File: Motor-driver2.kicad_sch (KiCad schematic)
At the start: 30 parts, among them J12 PINHD_1x4_Male, J15 PINHD_1x4_Male, U4 DRV8825PWP, U5 DRV8825PWP

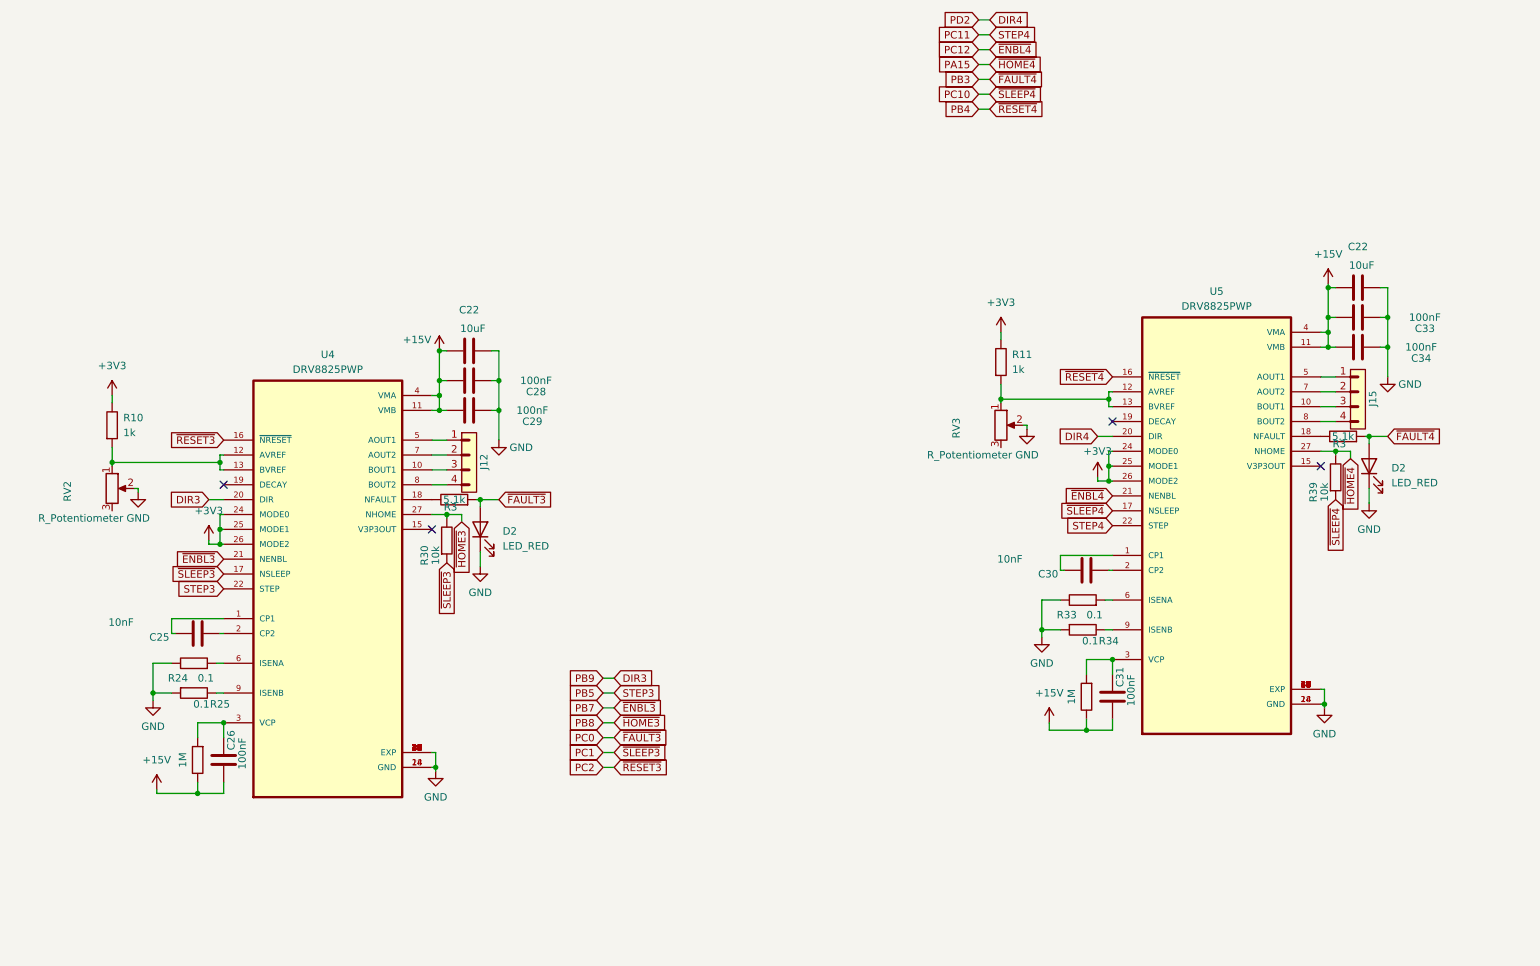
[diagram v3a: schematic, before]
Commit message: placed jlcpcb basic buttons and rerouted unchristliche wires
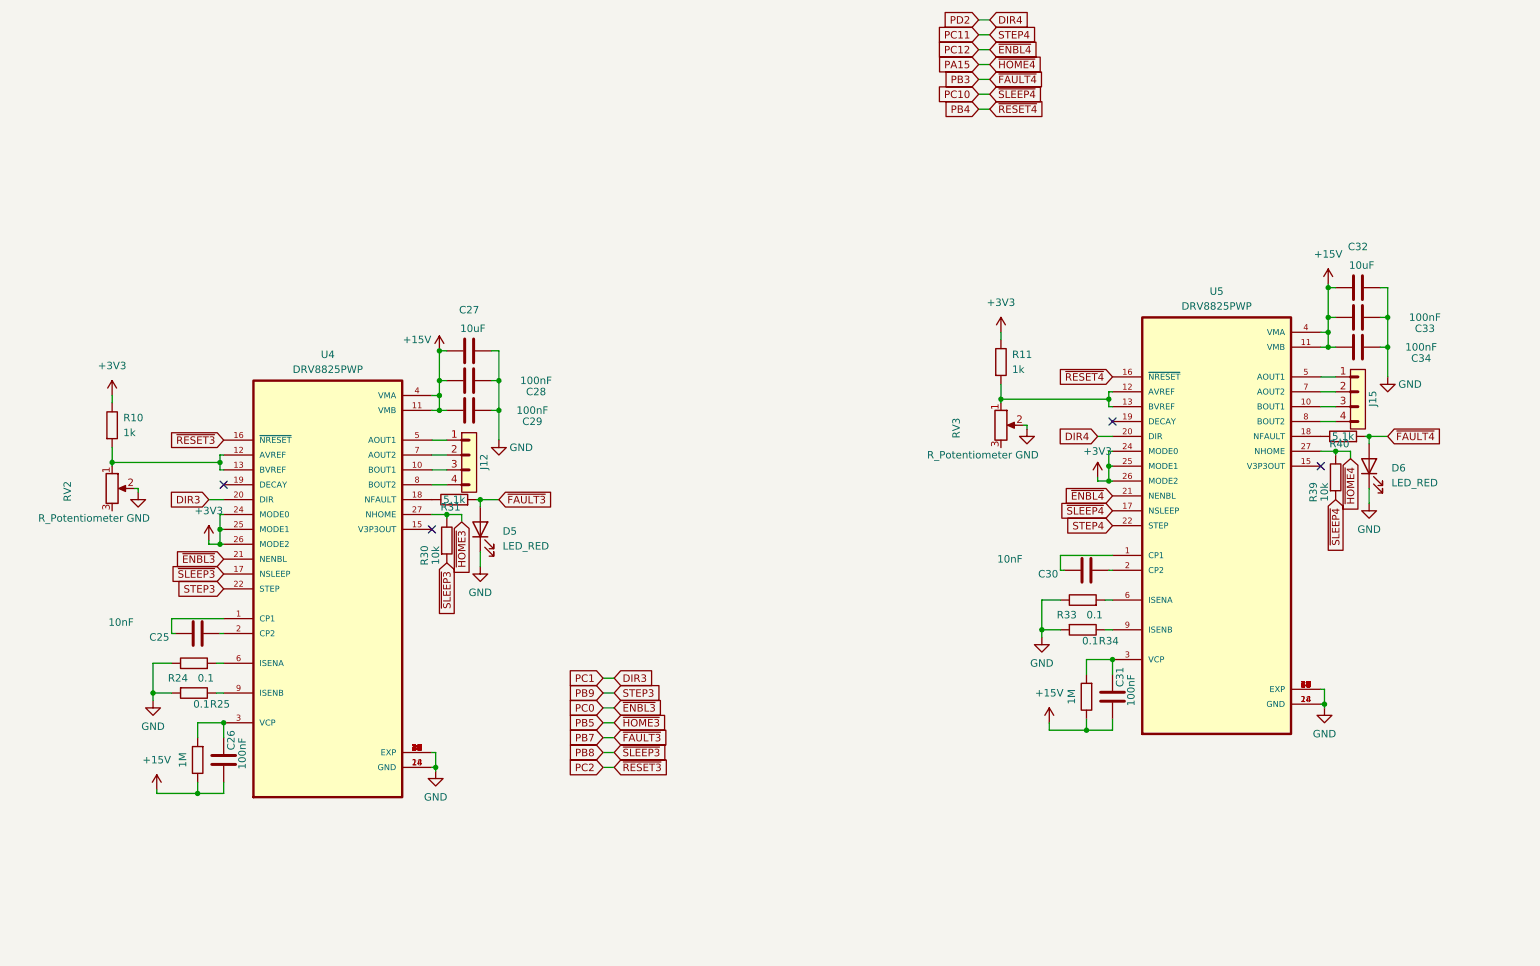
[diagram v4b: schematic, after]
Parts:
- renumbered C22 to C27, C22 to C32, D2 to D5, D2 to D6, R3 to R31, R3 to R40
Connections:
- net PC1 is gone; now on net PB8: R30.1, U4.17 (NSLEEP)
- net PB5: now also R30.2, U4.27 (NHOME); no longer U4.22 (STEP)
- net PB7: now also D5.2 (A), R31.1; no longer U4.21 (NENBL)
- net PB8: no longer R30.2, U4.27 (NHOME)
- net PC0: now also U4.21 (NENBL); no longer D5.2 (A), R31.1
- new net PB9: U4.22 (STEP)

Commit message: added pins for motor edge sensors, reroutet driver modules, removed module potentiometer, made everything more compact, fixed labels
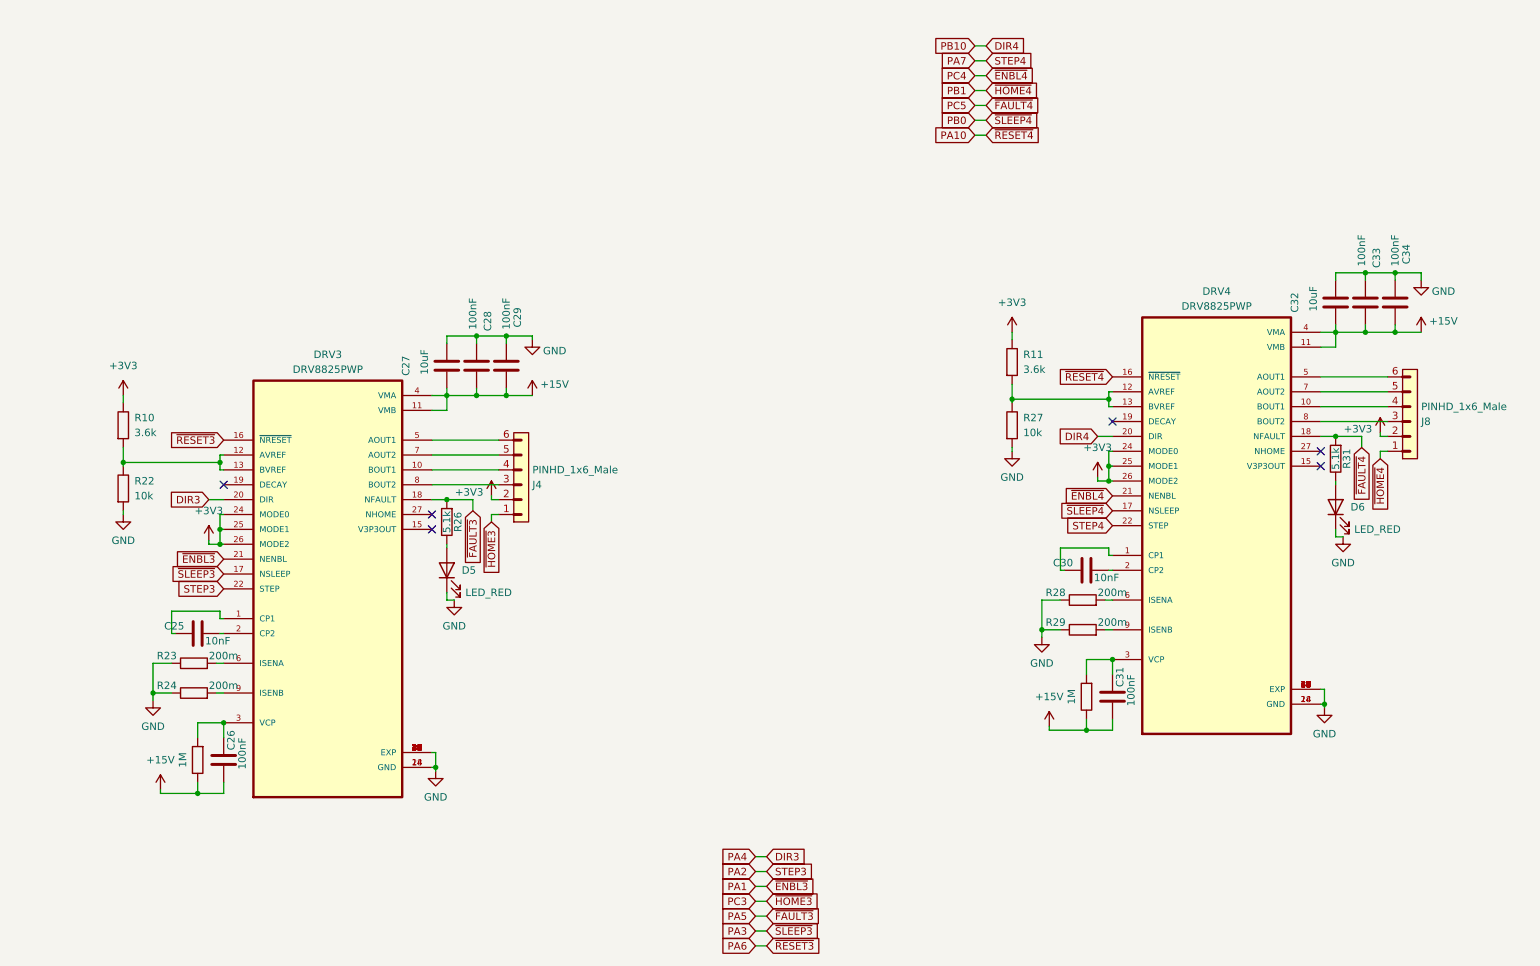
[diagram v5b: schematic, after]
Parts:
- removed J12, J15: PINHD_1x4_Male, Connector_PinHeader_2.54mm:PinHeader_1x04_P2.54mm_Vertical, symbol PCM_SL_Pin_Headers:PINHD_1x4_Male
- removed R33, R34: 0.1, Resistor_SMD:R_1206_3216Metric, symbol PCM_SL_Devices:Resistor
- removed R35: 1M, Resistor_SMD:R_0805_2012Metric, symbol PCM_SL_Devices:Resistor
- removed R39: 10k, Resistor_SMD:R_0805_2012Metric, symbol PCM_SL_Devices:Resistor
- removed R40: 5.1k, Resistor_SMD:R_0805_2012Metric, symbol PCM_SL_Devices:Resistor
- removed RV2, RV3: R_Potentiometer, poti:3386P1473LF, symbol Device:R_Potentiometer
- added J4, J8: PINHD_1x6_Male, Connector_PinHeader_2.54mm:PinHeader_1x06_P2.54mm_Vertical, symbol PCM_SL_Pin_Headers:PINHD_1x6_Male
- added R22, R27: 10k, Resistor_SMD:R_0805_2012Metric, symbol PCM_SL_Devices:Resistor
- added R23, R28, R29: 200m, Resistor_SMD:R_0402_1005Metric, symbol PCM_SL_Devices:Resistor
- R10, R11: value 1k -> 3.6k
- R24: value 0.1 -> 200m; footprint Resistor_SMD:R_1206_3216Metric -> Resistor_SMD:R_0402_1005Metric
- R25: value 0.1 -> 1M; footprint Resistor_SMD:R_1206_3216Metric -> Resistor_SMD:R_0805_2012Metric
- R26: value 1M -> 5.1k
- R30: value 10k -> 1M
- renumbered U4 to DRV3, U5 to DRV4
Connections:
- net PB3 is gone; now on an unnamed net: D6.2 (A)
- net +15V: now also R25.2, R30.2; no longer R26.2
- net +3V3: now also J4.2, J8.2
- net GND: now also R22.1, R23.2, R27.1, R28.2, R29.2; no longer R25.1
- net at DRV4.5 (AOUT1): now also J8.6
- net at DRV4.7 (AOUT2): now also J8.5
- net at DRV4.10 (BOUT1): now also J8.4
- net at DRV4.8 (BOUT2): now also J8.3
- net PC5: now reaches DRV4.18 (NFAULT)
- net PC5: now also R31.1
- net at DRV3.12 (AVREF), DRV3.13 (BVREF), R10.1: now also R22.2
- net at DRV4.6 (ISENA): now also R28.1
- net at C31.2, DRV4.3 (VCP): now also R30.1
- net at C26.2, DRV3.3 (VCP): now also R25.1; no longer R26.1
- net at DRV4.12 (AVREF), DRV4.13 (BVREF), R11.1: now also R27.2
- net at R31.2: no longer DRV3.18 (NFAULT)
- net at DRV3.10 (BOUT1): now also J4.4
- net at DRV3.5 (AOUT1): now also J4.6
- net at DRV3.6 (ISENA): now also R23.1; no longer R24.1
- net at DRV3.7 (AOUT2): now also J4.5
- net at DRV3.8 (BOUT2): now also J4.3
- net at DRV3.9 (ISENB): now also R24.1; no longer R25.2
- net at DRV4.9 (ISENB): now also R29.1
- net PA15: no longer names the net of DRV4.27 (NHOME)
- net PB4 renamed PA10
- net PB5: no longer names the net of DRV3.27 (NHOME)
- net PB5: no longer R30.2
- net PB7: no longer names the net of D5.2 (A)
- net PB7: now also R26.2; no longer R31.1
- net PB8 renamed PA3
- net PA3: no longer R30.1
- net PB9 renamed PA2
- net PC0 renamed PA1
- net PC10 renamed PB0
- net PC11 renamed PA7
- net PC12 renamed PC4
- net PC2 renamed PA6
- new net PA5: DRV3.18 (NFAULT), R26.1
- new net PB1: J8.1
- new net PC3: J4.1
- no-connect marks 4 -> 6
